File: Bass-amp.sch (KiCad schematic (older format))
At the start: 13 parts, among them U1 ECC81

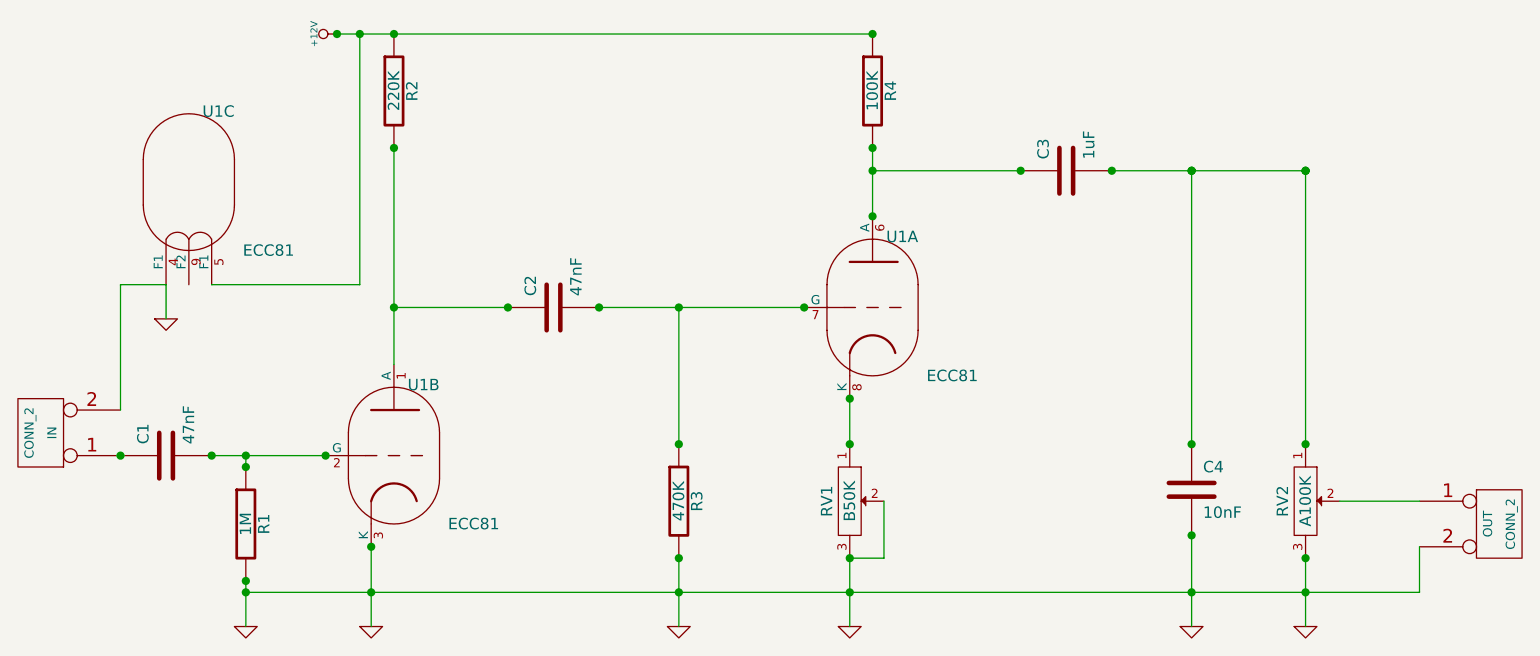
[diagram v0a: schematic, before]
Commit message: more work on PCB layout, changed to ECC82
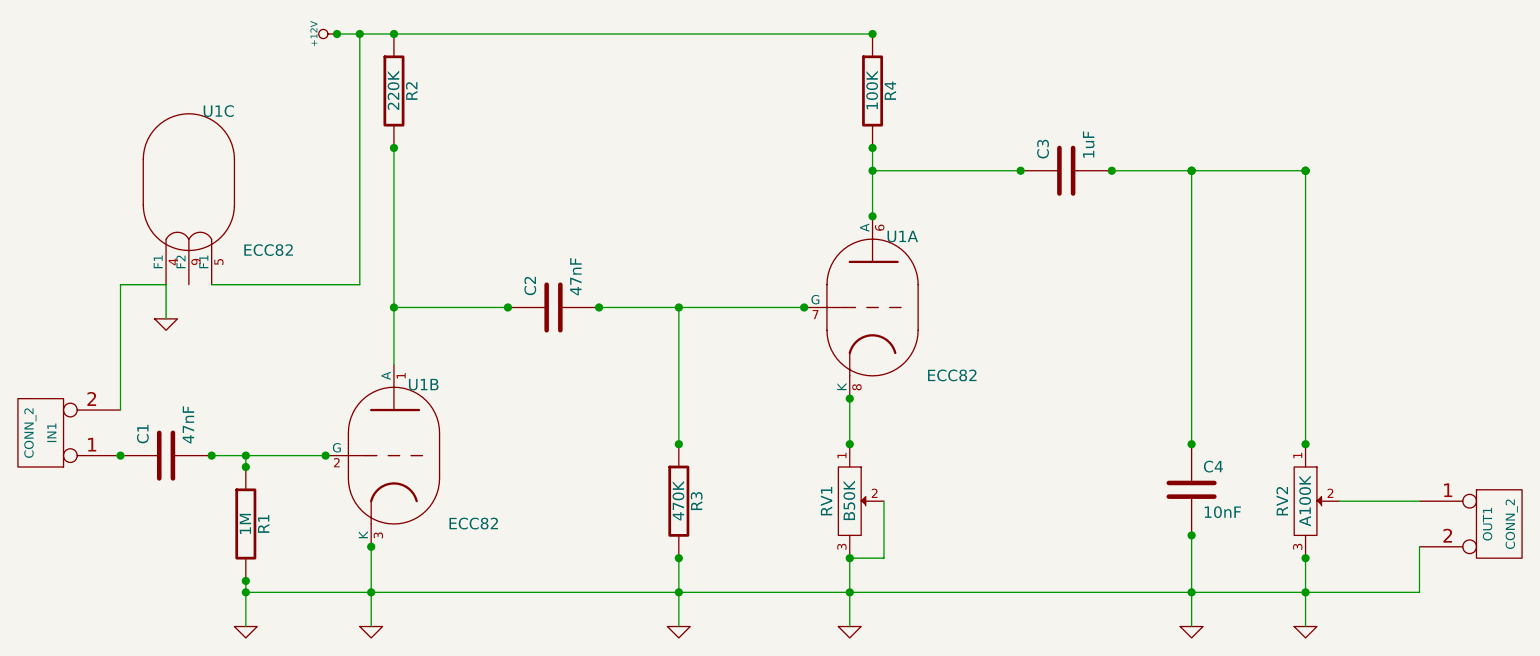
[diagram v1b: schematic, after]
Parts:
- U1: value ECC81 -> ECC82
- renumbered IN to IN1, OUT to OUT1
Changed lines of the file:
@@
-EESchema Schematic File Version 2  date Sun 22 Dec 2013 22:21:06 NZDT
+EESchema Schematic File Version 2  date Tue 24 Dec 2013 22:38:24 NZDT
 LIBS:power
 LIBS:device
@@
 encoding utf-8
 Sheet 1 1
-Title ""
-Date "22 dec 2013"
+Title "Valvecaster clone"
+Date "24 dec 2013"
 Rev ""
 Comp ""
@@
 	3400 3300 3400 3850
 $Comp
-L CONN_2 OUT
+L CONN_2 OUT1
 U 1 1 52B6AD16
 P 9450 4350
-F 0 "OUT" V 9400 4350 40  0000 C CNN
+F 0 "OUT1" V 9400 4350 40  0000 C CNN
 F 1 "CONN_2" V 9500 4350 40  0000 C CNN
 	1    9450 4350
@@
 $EndComp
 $Comp
-L CONN_2 IN
+L CONN_2 IN1
 U 1 1 52B6ACE1
 P 3050 3950
-F 0 "IN" V 3000 3950 40  0000 C CNN
+F 0 "IN1" V 3000 3950 40  0000 C CNN
 F 1 "CONN_2" V 3100 3950 40  0000 C CNN
 	1    3050 3950
@@
 $EndComp
 $Comp
-L GND #PWR1
+L GND #PWR01
 U 1 1 52B6A709
 P 3600 3450
-F 0 "#PWR1" H 3600 3450 30  0001 C CNN
+F 0 "#PWR01" H 3600 3450 30  0001 C CNN
 F 1 "GND" H 3600 3380 30  0001 C CNN
 	1    3600 3450
@@
 P 3700 2850
 F 0 "U1" H 3830 3160 50  0000 C CNN
-F 1 "ECC81" H 4050 2550 50  0000 C CNN
+F 1 "ECC82" H 4050 2550 50  0000 C CNN
 F 2 "VALVE-NOVAL_P" H 3970 2450 50  0001 C CNN
 	3    3700 2850
@@
 $EndComp
 $Comp
-L GND #PWR8
+L GND #PWR02
 U 1 1 52B54168
 P 8600 4800
-F 0 "#PWR8" H 8600 4800 30  0001 C CNN
+F 0 "#PWR02" H 8600 4800 30  0001 C CNN
 F 1 "GND" H 8600 4730 30  0001 C CNN
 	1    8600 4800
@@
 $EndComp
 $Comp
-L GND #PWR7
+L GND #PWR03
 U 1 1 52B5415A
 P 8100 4800
-F 0 "#PWR7" H 8100 4800 30  0001 C CNN
+F 0 "#PWR03" H 8100 4800 30  0001 C CNN
 F 1 "GND" H 8100 4730 30  0001 C CNN
 	1    8100 4800
@@
 $EndComp
 $Comp
-L GND #PWR5
+L GND #PWR04
 U 1 1 52B5414F
 P 5850 4800
-F 0 "#PWR5" H 5850 4800 30  0001 C CNN
+F 0 "#PWR04" H 5850 4800 30  0001 C CNN
 F 1 "GND" H 5850 4730 30  0001 C CNN
 	1    5850 4800
@@
 $EndComp
 $Comp
-L GND #PWR6
+L GND #PWR05
 U 1 1 52B54149
 P 6600 4800
-F 0 "#PWR6" H 6600 4800 30  0001 C CNN
+F 0 "#PWR05" H 6600 4800 30  0001 C CNN
 F 1 "GND" H 6600 4730 30  0001 C CNN
 	1    6600 4800
@@
 $EndComp
 $Comp
-L GND #PWR2
+L GND #PWR06
 U 1 1 52B5413E
 P 3950 4800
-F 0 "#PWR2" H 3950 4800 30  0001 C CNN
+F 0 "#PWR06" H 3950 4800 30  0001 C CNN
 F 1 "GND" H 3950 4730 30  0001 C CNN
 	1    3950 4800
@@
 $EndComp
 $Comp
-L GND #PWR4
+L GND #PWR07
 U 1 1 52B54133
 P 4500 4800
-F 0 "#PWR4" H 4500 4800 30  0001 C CNN
+F 0 "#PWR07" H 4500 4800 30  0001 C CNN
 F 1 "GND" H 4500 4730 30  0001 C CNN
 	1    4500 4800
@@
 $EndComp
 $Comp
-L +12V #PWR3
+L +12V #PWR08
 U 1 1 52B53F99
 P 4350 2200
-F 0 "#PWR3" H 4350 2150 20  0001 C CNN
+F 0 "#PWR08" H 4350 2150 20  0001 C CNN
 F 1 "+12V" H 4350 2300 30  0000 C CNN
 	1    4350 2200
@@
 P 6700 3400
 F 0 "U1" H 6830 3710 50  0000 C CNN
-F 1 "ECC81" H 7050 3100 50  0000 C CNN
+F 1 "ECC82" H 7050 3100 50  0000 C CNN
 F 2 "VALVE-NOVAL_P" H 6970 3000 50  0001 C CNN
 	1    6700 3400
@@
 P 4600 4050
 F 0 "U1" H 4730 4360 50  0000 C CNN
-F 1 "ECC81" H 4950 3750 50  0000 C CNN
+F 1 "ECC82" H 4950 3750 50  0000 C CNN
 F 2 "VALVE-NOVAL_P" H 4870 3650 50  0001 C CNN
 	2    4600 4050
